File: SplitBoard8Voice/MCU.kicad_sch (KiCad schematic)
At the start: 88 parts, among them J401 PWR, J402 DATA, J403 SWD Header, J404 MIDI_In, J405 Micro_SD_Card_Det2, J406 MIDI_Out, J407 MIDI_Thru, SW401 RST, SW402 BOOT, U401 STM32F411RETx, U404 74HC04, U405 6N138, Y401 16MHz, Y402 32.768kHZ

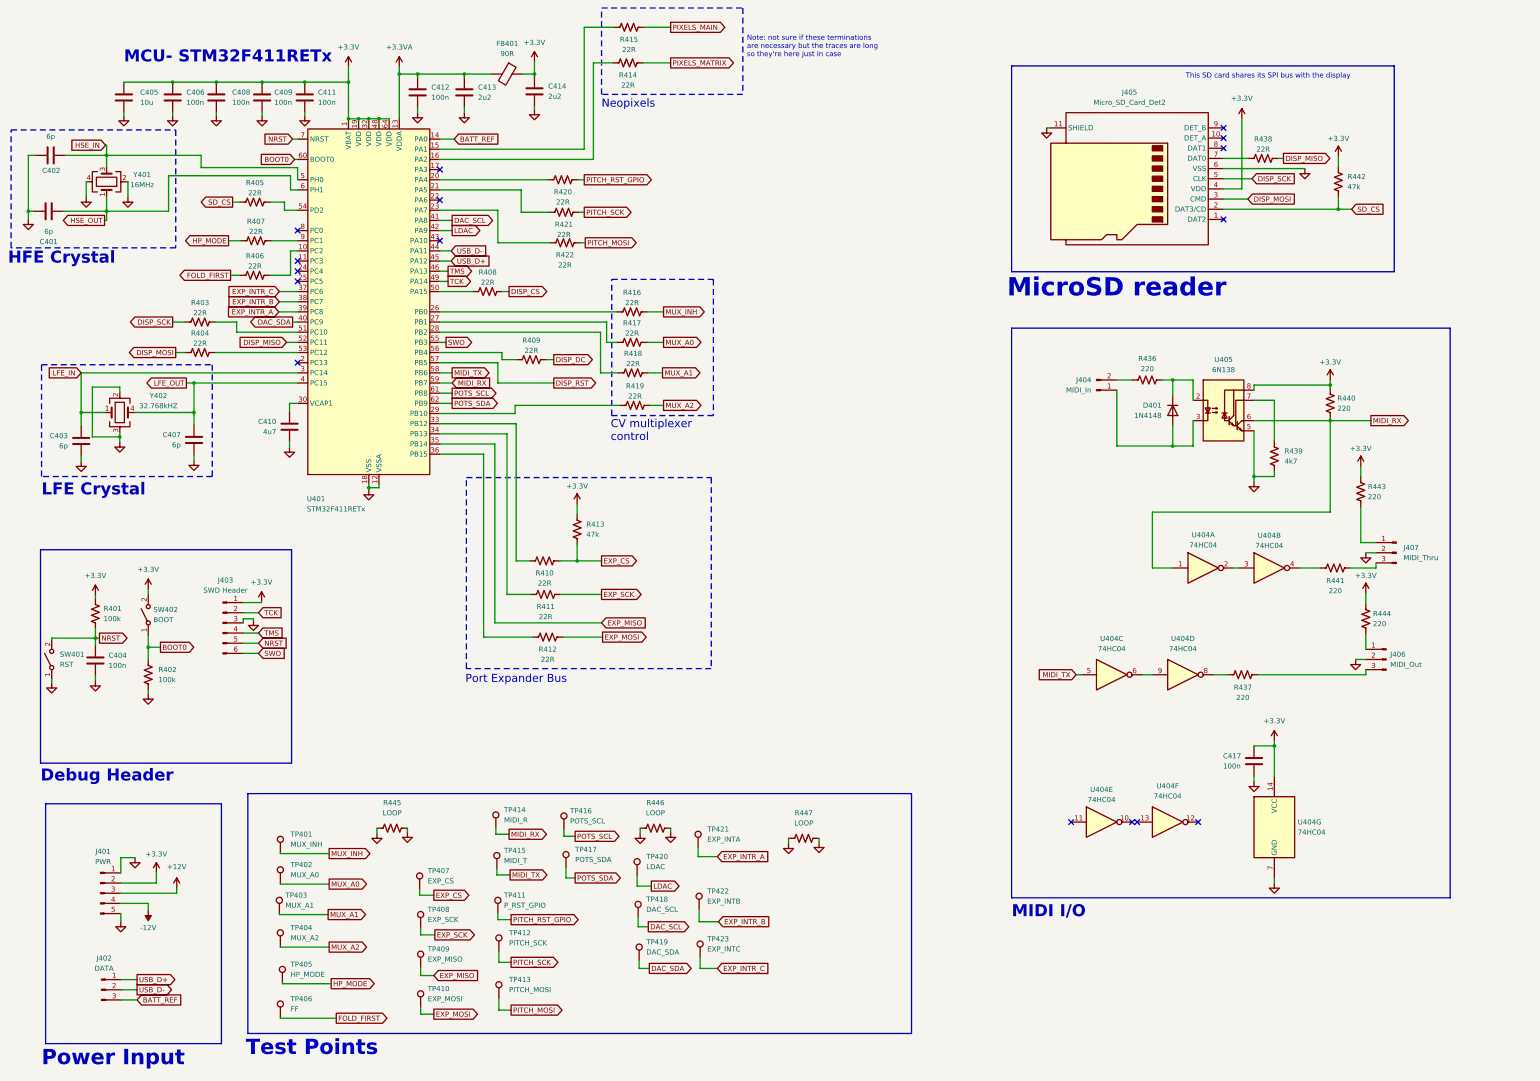
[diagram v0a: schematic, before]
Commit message: Eurorack power capability sorted out
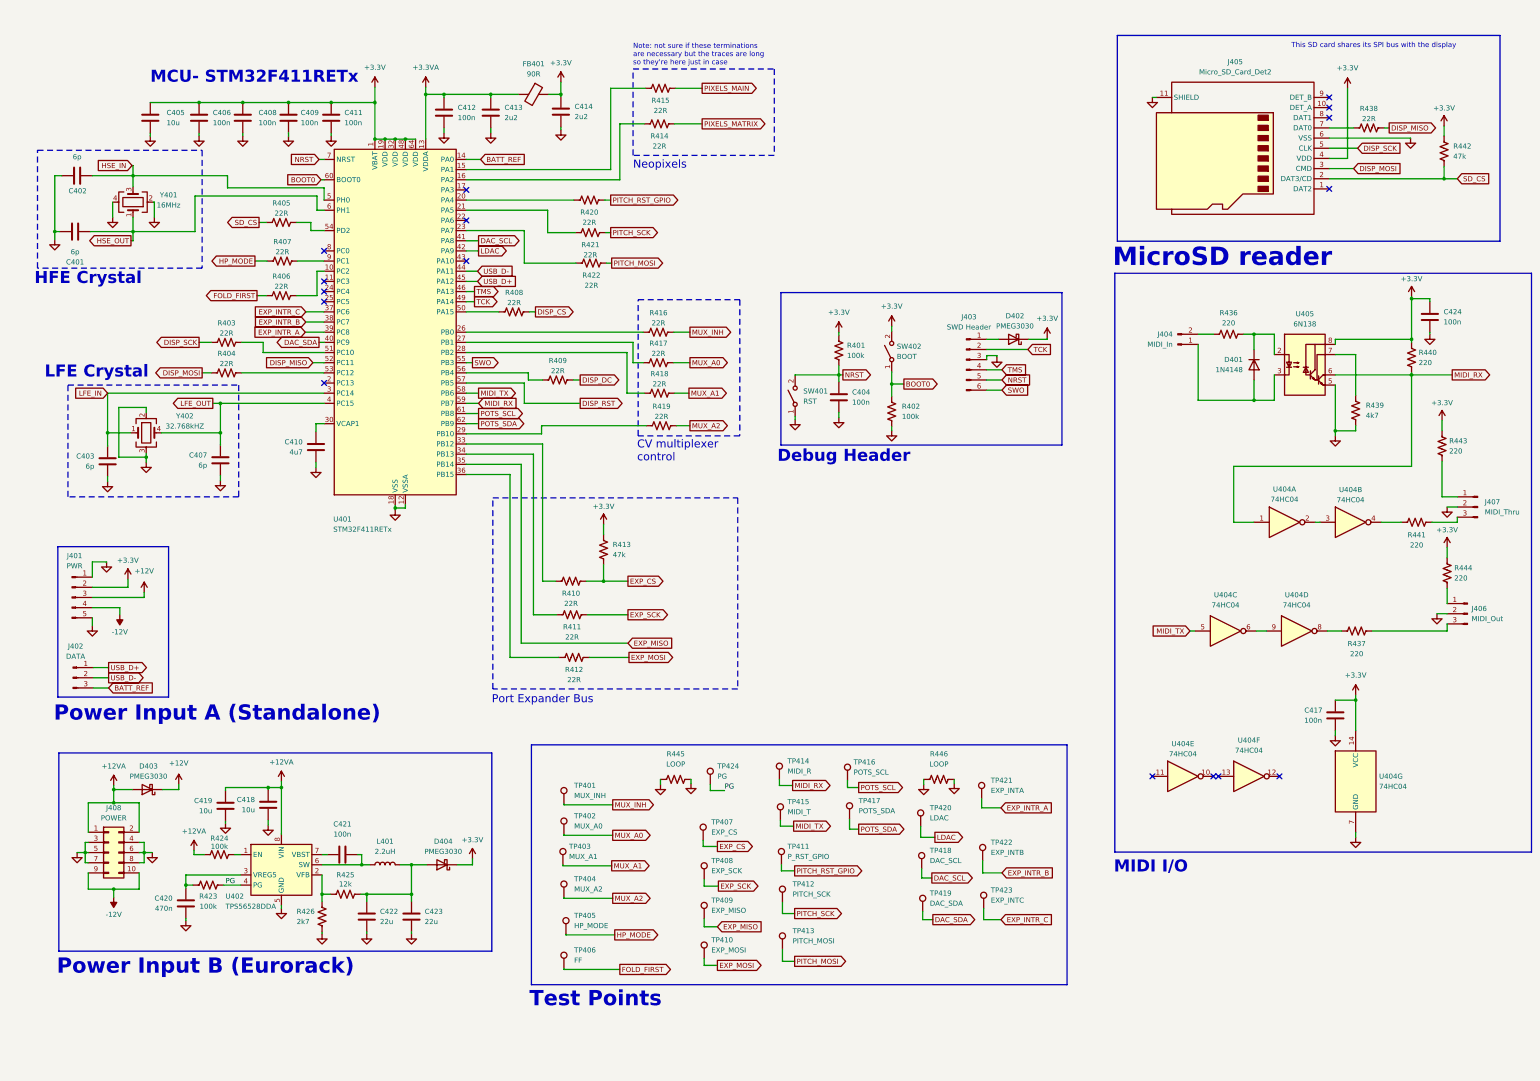
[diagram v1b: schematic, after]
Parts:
- removed R447: LOOP, Resistor_THT:R_Axial_DIN0204_L3.6mm_D1.6mm_P5.08mm_Horizontal, symbol Device:R_US
- added C418, C419: 10u, Capacitor_SMD:C_0805_2012Metric, symbol Device:C
- added C420: 470n, Capacitor_SMD:C_0805_2012Metric, symbol Device:C
- added C421, C424: 100n, Capacitor_SMD:C_0805_2012Metric, symbol Device:C
- added C422, C423: 22u, Capacitor_SMD:C_0805_2012Metric, symbol Device:C
- added D402, D403, D404: PMEG3030, Diode_SMD:D_SOD-123, symbol Device:D_Schottky
- added J408: POWER, Connector_PinHeader_2.54mm:PinHeader_2x05_P2.54mm_Vertical, symbol Connector_Generic:Conn_02x05_Odd_Even
- added L401: 2.2uH, Inductor_SMD:L_Abracon_ASPI-4030S, symbol Device:L
- added R423, R424: 100k, Resistor_SMD:R_0805_2012Metric, symbol Device:R_US
- added R425: 12k, Resistor_SMD:R_0805_2012Metric, symbol Device:R_US
- added R426: 2k7, Resistor_SMD:R_0805_2012Metric, symbol Device:R_US
- added TP424: PG, TestPoint:TestPoint_THTPad_D1.0mm_Drill0.5mm_VAL, symbol Connector:TestPoint
- added U402: TPS56528DDA, Package_SO:Texas_HSOP-8-1EP_3.9x4.9mm_P1.27mm_ThermalVias, symbol Regulator_Switching:TPS56528DDA
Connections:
- net +12V: now also D403.1 (K)
- net +3.3V: now also C424.1, D402.1 (K), D404.1 (K); no longer J403.1 (Pin_1)
- net -12V: now also J408.10 (Pin_10), J408.9 (Pin_9)
- net GND: now also C418.2, C419.2, C420.2, C422.2, C423.2, C424.2, J408.3 (Pin_3), J408.4 (Pin_4), J408.5 (Pin_5), J408.6 (Pin_6), J408.7 (Pin_7), J408.8 (Pin_8), R426.2, U402.5 (GND), U402.9 (GND)
- new net: R425.1, R426.1, U402.2 (VFB)
- new net: C422.1, C423.1, D404.2 (A), L401.2, R425.2
- new net: C421.1, L401.1, U402.6 (SW)
- new net: C421.2, U402.7 (VBST)
- new net: D402.2 (A), J403.1 (Pin_1)
- new net: C420.1, R423.1, U402.3 (VREG5)
- new net: R424.2, U402.1 (EN)
- new net +12VA: C418.1, C419.1, D403.2 (A), J408.1 (Pin_1), J408.2 (Pin_2), R424.1, U402.8 (VIN)
- new net PG: R423.2, TP424.1, U402.4 (PG)
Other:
- note added: "Power Input A (Standalone)"
- note added: "Power Input B (Eurorack)"
- note removed: "Power Input"
- moved on the sheet: C401, C402, C403, C404, C405, C406, C407, C408, C409, C410, C411, C412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

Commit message: transfer vias and test points added
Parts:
- TP401, TP402, TP403, TP404, TP405, TP406: footprint TestPoint:TestPoint_THTPad_D1.5mm_Drill0.7mm_VAL -> TestPoint:TestPoint_THTPad_D1.0mm_Drill0.5mm_VAL
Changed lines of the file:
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@@
 		(exclude_from_sim no)
 		(in_bom no)
-		(on_board no)
+		(on_board yes)
 		(dnp no)
 		(fields_autoplaced yes)
@@
 			)
 		)
-		(property "Footprint" "TestPoint:TestPoint_THTPad_D1.5mm_Drill0.7mm_VAL"
+		(property "Footprint" "TestPoint:TestPoint_THTPad_D1.0mm_Drill0.5mm_VAL"
 			(at 156.972 228.854 0)
 			(effects
@@
 		(exclude_from_sim no)
 		(in_bom no)
-		(on_board no)
+		(on_board yes)
 		(dnp no)
 		(fields_autoplaced yes)
@@
 		(exclude_from_sim no)
 		(in_bom no)
-		(on_board no)
+		(on_board yes)
 		(dnp no)
 		(fields_autoplaced yes)
@@
 			)
 		)
-		(property "Footprint" "TestPoint:TestPoint_THTPad_D1.5mm_Drill0.7mm_VAL"
+		(property "Footprint" "TestPoint:TestPoint_THTPad_D1.0mm_Drill0.5mm_VAL"
 			(at 157.226 221.234 0)
 			(effects
@@
 		(exclude_from_sim no)
 		(in_bom no)
-		(on_board no)
+		(on_board yes)
 		(dnp no)
 		(fields_autoplaced yes)
@@
 		(exclude_from_sim no)
 		(in_bom no)
-		(on_board no)
+		(on_board yes)
 		(dnp no)
 		(fields_autoplaced yes)
@@
 		(exclude_from_sim no)
 		(in_bom no)
-		(on_board no)
+		(on_board yes)
 		(dnp no)
 		(fields_autoplaced yes)
@@
 			)
 		)
-		(property "Footprint" "TestPoint:TestPoint_THTPad_D1.5mm_Drill0.7mm_VAL"
+		(property "Footprint" "TestPoint:TestPoint_THTPad_D1.0mm_Drill0.5mm_VAL"
 			(at 157.226 254.762 0)
 			(effects
@@
 		(exclude_from_sim no)
 		(in_bom no)
-		(on_board no)
+		(on_board yes)
 		(dnp no)
 		(fields_autoplaced yes)
@@
 		(exclude_from_sim no)
 		(in_bom no)
-		(on_board no)
+		(on_board yes)
 		(dnp no)
 		(fields_autoplaced yes)
@@
 			)
 		)
-		(property "Footprint" "TestPoint:TestPoint_THTPad_D1.5mm_Drill0.7mm_VAL"
+		(property "Footprint" "TestPoint:TestPoint_THTPad_D1.0mm_Drill0.5mm_VAL"
 			(at 157.226 213.614 0)
 			(effects
@@
 		(exclude_from_sim no)
 		(in_bom no)
-		(on_board no)
+		(on_board yes)
 		(dnp no)
 		(fields_autoplaced yes)
@@
 			)
 		)
-		(property "Footprint" "TestPoint:TestPoint_THTPad_D1.5mm_Drill0.7mm_VAL"
+		(property "Footprint" "TestPoint:TestPoint_THTPad_D1.0mm_Drill0.5mm_VAL"
 			(at 157.734 246.126 0)
 			(effects
@@
 		(exclude_from_sim no)
 		(in_bom no)
-		(on_board no)
+		(on_board yes)
 		(dnp no)
 		(fields_autoplaced yes)
@@
 		(exclude_from_sim no)
 		(in_bom no)
-		(on_board no)
+		(on_board yes)
 		(dnp no)
 		(fields_autoplaced yes)
@@
 		(exclude_from_sim no)
 		(in_bom no)
-		(on_board no)
+		(on_board yes)
 		(dnp no)
 		(fields_autoplaced yes)
@@
 		(exclude_from_sim no)
 		(in_bom no)
-		(on_board no)
+		(on_board yes)
 		(dnp no)
 		(fields_autoplaced yes)
@@
 		(exclude_from_sim no)
 		(in_bom no)
-		(on_board no)
+		(on_board yes)
 		(dnp no)
 		(fields_autoplaced yes)
@@
 		(exclude_from_sim no)
 		(in_bom no)
-		(on_board no)
+		(on_board yes)
 		(dnp no)
 		(fields_autoplaced yes)
@@
 		(exclude_from_sim no)
 		(in_bom no)
-		(on_board no)
+		(on_board yes)
 		(dnp no)
 		(fields_autoplaced yes)
@@
 		(exclude_from_sim no)
 		(in_bom no)
-		(on_board no)
+		(on_board yes)
 		(dnp no)
 		(fields_autoplaced yes)
@@
 		(exclude_from_sim no)
 		(in_bom no)
-		(on_board no)
+		(on_board yes)
 		(dnp no)
 		(fields_autoplaced yes)
@@
 			)
 		)
-		(property "Footprint" "TestPoint:TestPoint_THTPad_D1.5mm_Drill0.7mm_VAL"
+		(property "Footprint" "TestPoint:TestPoint_THTPad_D1.0mm_Drill0.5mm_VAL"
 			(at 157.226 236.982 0)
 			(effects
@@
 		(exclude_from_sim no)
 		(in_bom no)
-		(on_board no)
+		(on_board yes)
 		(dnp no)
 		(fields_autoplaced yes)
@@
 		(exclude_from_sim no)
 		(in_bom no)
-		(on_board no)
+		(on_board yes)
 		(dnp no)
 		(fields_autoplaced yes)
@@
 		(exclude_from_sim no)
 		(in_bom no)
-		(on_board no)
+		(on_board yes)
 		(dnp no)
 		(fields_autoplaced yes)
@@
 		(exclude_from_sim no)
 		(in_bom no)
-		(on_board no)
+		(on_board yes)
 		(dnp no)
 		(fields_autoplaced yes)
@@
 		(exclude_from_sim no)
 		(in_bom no)
-		(on_board no)
+		(on_board yes)
 		(dnp no)
 		(fields_autoplaced yes)
@@
 		(exclude_from_sim no)
 		(in_bom no)
-		(on_board no)
+		(on_board yes)
 		(dnp no)
 		(fields_autoplaced yes)

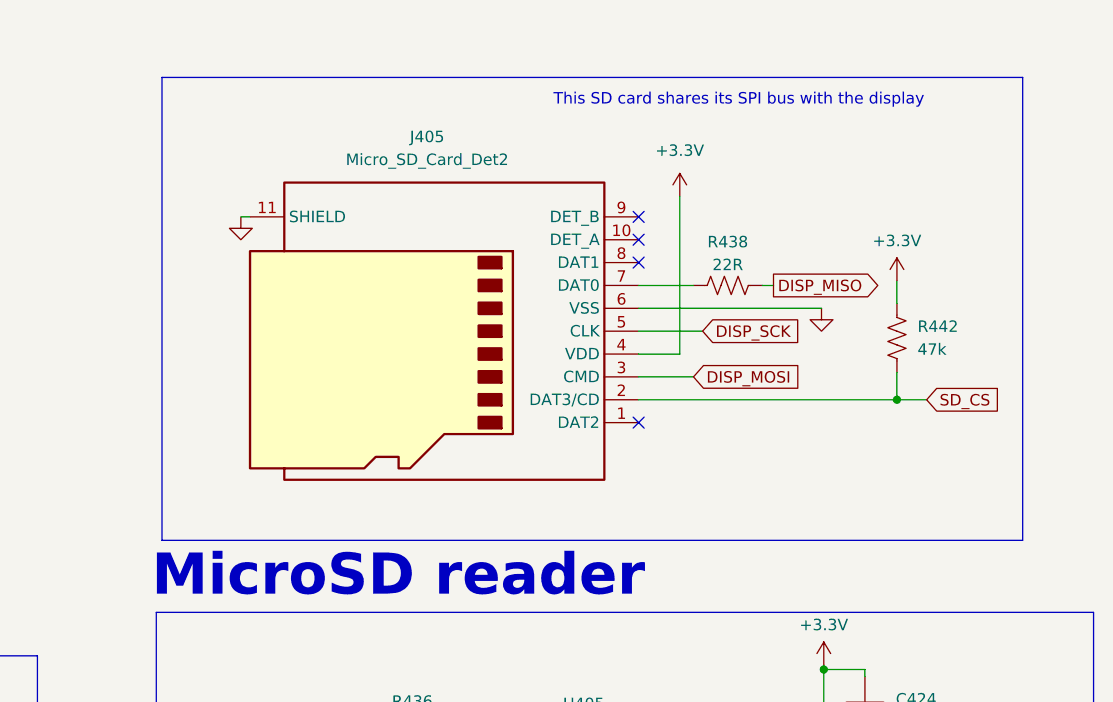
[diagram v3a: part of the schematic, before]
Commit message: silkscreen stuff, spacing cleanup
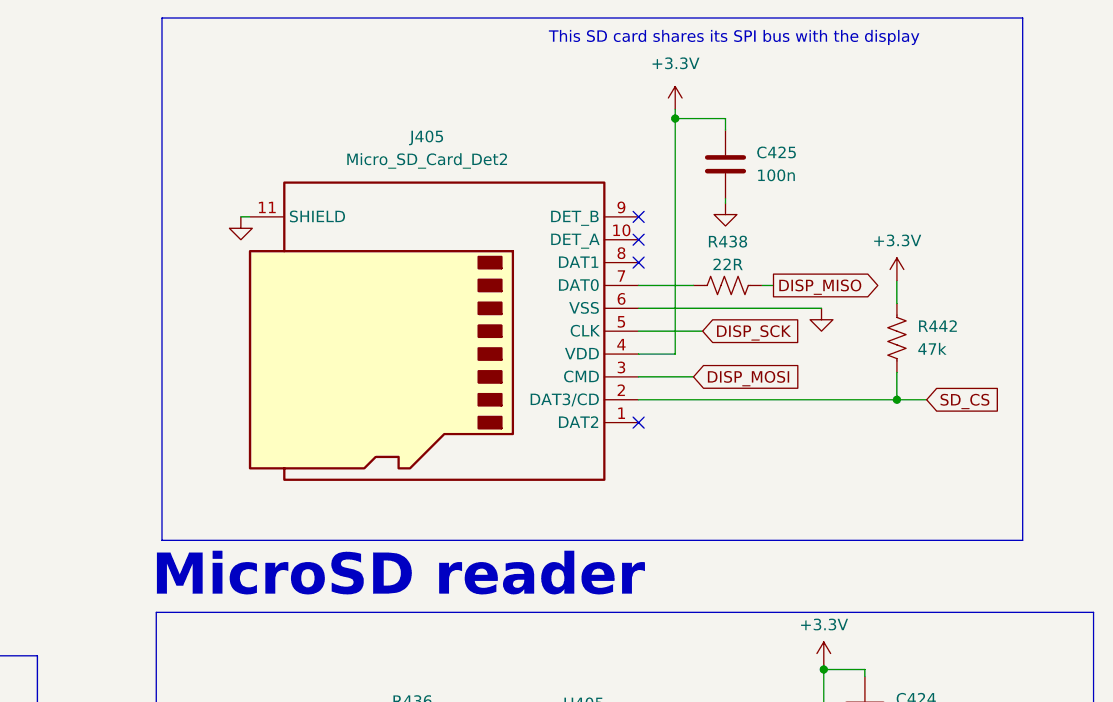
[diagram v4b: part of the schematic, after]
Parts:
- added C425: 100n, Capacitor_SMD:C_0805_2012Metric, symbol Device:C
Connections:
- net +3.3V: now also C425.1
- net GND: now also C425.2
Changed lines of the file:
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@@
 	)
 	(junction
+		(at 347.472 26.162)
+		(diameter 0)
+		(color 0 0 0 0)
+	)
+	(junction
 		(at 104.902 38.354)
 		(diameter 0)
@@
 	(wire
 		(pts
-			(xy 347.98 34.798) (xy 347.98 52.324)
+			(xy 347.472 25.146) (xy 347.472 26.162)
 		)
 		(stroke
@@
 	(wire
 		(pts
-			(xy 347.98 52.324) (xy 343.408 52.324)
+			(xy 347.472 52.324) (xy 343.408 52.324)
 		)
 		(stroke
@@
 	(wire
 		(pts
+			(xy 353.06 26.162) (xy 347.472 26.162)
+		)
+		(stroke
+			(width 0)
+			(type default)
+		)
+	)
+	(wire
+		(pts
 			(xy 66.294 113.538) (xy 92.202 113.538)
 		)
@@
 	(wire
 		(pts
+			(xy 353.06 35.052) (xy 353.06 35.56)
+		)
+		(stroke
+			(width 0)
+			(type default)
+		)
+	)
+	(wire
+		(pts
 			(xy 83.312 38.354) (xy 93.98 38.354)
 		)
@@
 	(wire
 		(pts
+			(xy 347.472 26.162) (xy 347.472 52.324)
+		)
+		(stroke
+			(width 0)
+			(type default)
+		)
+	)
+	(wire
+		(pts
 			(xy 127.762 123.698) (xy 146.812 123.698)
 		)
@@
 	(wire
 		(pts
+			(xy 353.06 27.432) (xy 353.06 26.162)
+		)
+		(stroke
+			(width 0)
+			(type default)
+		)
+	)
+	(wire
+		(pts
 			(xy 32.512 228.346) (xy 32.512 225.806)
 		)
@@
 	)
 	(rectangle
-		(start 290.449 21.59)
+		(start 290.449 14.986)
 		(end 386.08 73.025)
 		(stroke
@@
 	(text "This SD card shares its SPI bus with the display"
 		(exclude_from_sim no)
-		(at 375.158 24.892 0)
+		(at 374.65 18.034 0)
 		(effects
 			(font
@@
 	)
 	(symbol
+		(lib_id "Device:C")
+		(at 353.06 31.242 0)
+		(unit 1)
+		(exclude_from_sim no)
+		(in_bom yes)
+		(on_board yes)
+		(dnp no)
+		(property "Reference" "C425"
+			(at 356.489 29.972 0)
+			(effects
+				(font
+					(size 1.27 1.27)
+				)
+				(justify left)
+			)
+		)
+		(property "Value" "100n"
+			(at 356.489 32.512 0)
+			(effects
+				(font
+					(size 1.27 1.27)
+				)
+				(justify left)
+			)
+		)
+		(property "Footprint" "Capacitor_SMD:C_0805_2012Metric"
+			(at 354.0252 35.052 0)
+			(effects
+				(font
+					(size 1.27 1.27)
+				)
+				(hide yes)
+			)
+		)
+		(property "Datasheet" "~"
+			(at 353.06 31.242 0)
+			(effects
+				(font
+					(size 1.27 1.27)
+				)
+				(hide yes)
+			)
+		)
+		(property "Description" ""
+			(at 353.06 31.242 0)
+			(effects
+				(font
+					(size 1.27 1.27)
+				)
+				(hide yes)
+			)
+		)
+		(pin "1"
+		)
+		(pin "2"
+		)
+		(instances
+			(project "SplitBoard8Voice"
+				(path "/22649217-9810-470f-bc7b-6f743ad2b90e/3d9ecb3b-9556-42d6-955a-a32d9efd5d3a/5768bcf0-b140-469b-9875-216e6a4fbfeb"
+					(reference "C425")
+					(unit 1)
+				)
+			)
+		)
+	)
+	(symbol
 		(lib_id "Connector:TestPoint")
 		(at 151.892 228.854 0)
@@
 	(symbol
 		(lib_id "power:+3.3V")
-		(at 347.98 34.798 0)
+		(at 347.472 25.146 0)
 		(unit 1)
 		(exclude_from_sim no)
@@
 		(fields_autoplaced yes)
 		(property "Reference" "#PWR0494"
-			(at 347.98 38.608 0)
+			(at 347.472 28.956 0)
 			(effects
 				(font
@@
 		)
 		(property "Value" "+3.3V"
-			(at 347.98 29.718 0)
+			(at 347.472 20.066 0)
 			(effects
 				(font
@@
 		)
 		(property "Footprint" ""
-			(at 347.98 34.798 0)
+			(at 347.472 25.146 0)
 			(effects
 				(font
@@
 		)
 		(property "Datasheet" ""
-			(at 347.98 34.798 0)
+			(at 347.472 25.146 0)
 			(effects
 				(font
@@
 		)
 		(property "Description" ""
-			(at 347.98 34.798 0)
+			(at 347.472 25.146 0)
 			(effects
 				(font
@@
 					(unit 1)
 				)
+			)
+		)
+	)
+	(symbol
+		(lib_id "power:GND")
+		(at 353.06 35.56 0)
+		(unit 1)
+		(exclude_from_sim no)
+		(in_bom yes)
+		(on_board yes)
+		(dnp no)
+		(fields_autoplaced yes)
+		(property "Reference" "#PWR0840"
+			(at 353.06 41.91 0)
+			(effects
+				(font
+					(size 1.27 1.27)
+				)
+				(hide yes)
+			)
+		)
+		(property "Value" "GND"
+			(at 353.06 39.37 0)
+			(effects
+				(font
+					(size 1.27 1.27)
+				)
+				(hide yes)
+			)
+		)
+		(property "Footprint" ""
+			(at 353.06 35.56 0)
+			(effects
+				(font
+					(size 1.27 1.27)
+				)
+				(hide yes)
+			)
+		)
+		(property "Datasheet" ""
+			(at 353.06 35.56 0)
+			(effects
+				(font
+					(size 1.27 1.27)
+				)
+				(hide yes)
+			)
+		)
+		(property "Description" ""
+			(at 353.06 35.56 0)
+			(effects
+				(font
+					(size 1.27 1.27)
+				)
+				(hide yes)
+			)
+		)
+		(pin "1"
+		)
+		(instances
+			(project "SplitBoard8Voice"
+				(path "/22649217-9810-470f-bc7b-6f743ad2b90e/3d9ecb3b-9556-42d6-955a-a32d9efd5d3a/5768bcf0-b140-469b-9875-216e6a4fbfeb"
+					(reference "#PWR0840")
+					(unit 1)
+				)
